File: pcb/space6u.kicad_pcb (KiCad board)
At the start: 2 copper layers, 116.7 x 45.2 mm, 7 parts, among them U1 Seeeduino Xiao rp2040

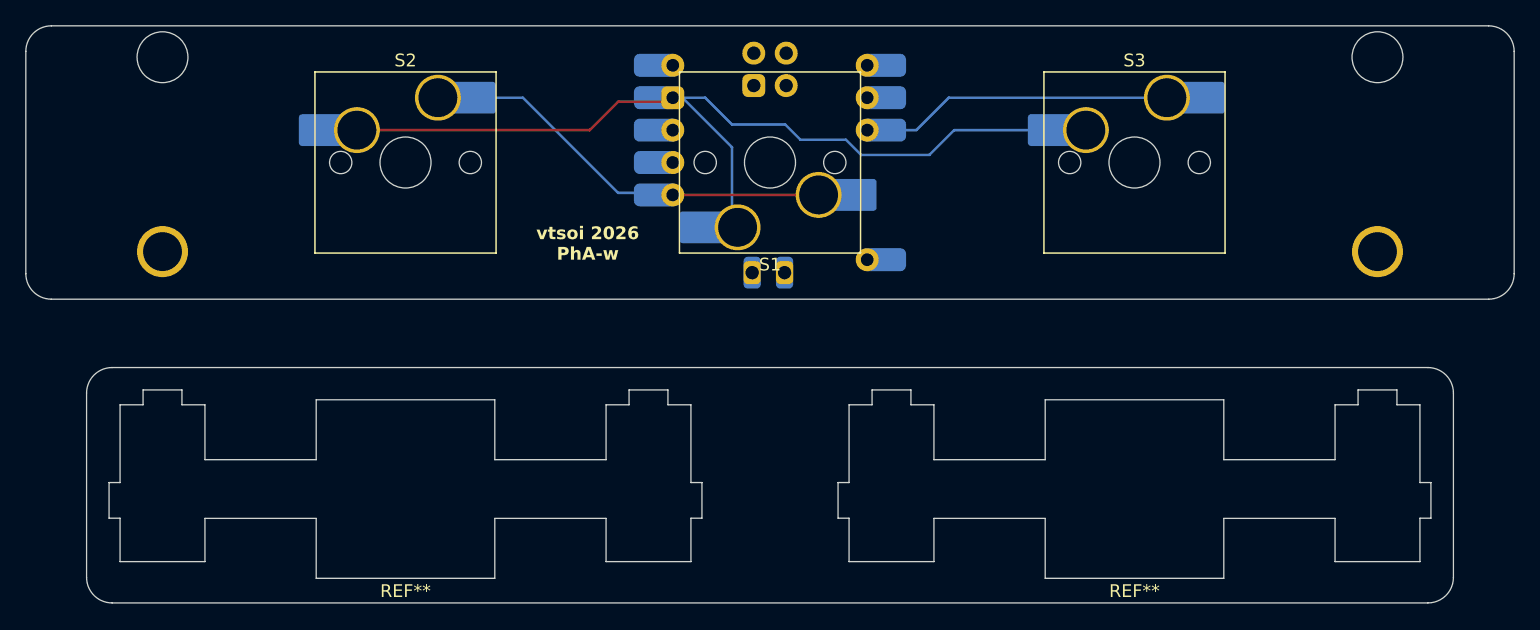
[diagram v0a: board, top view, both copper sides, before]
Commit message: plate and case files
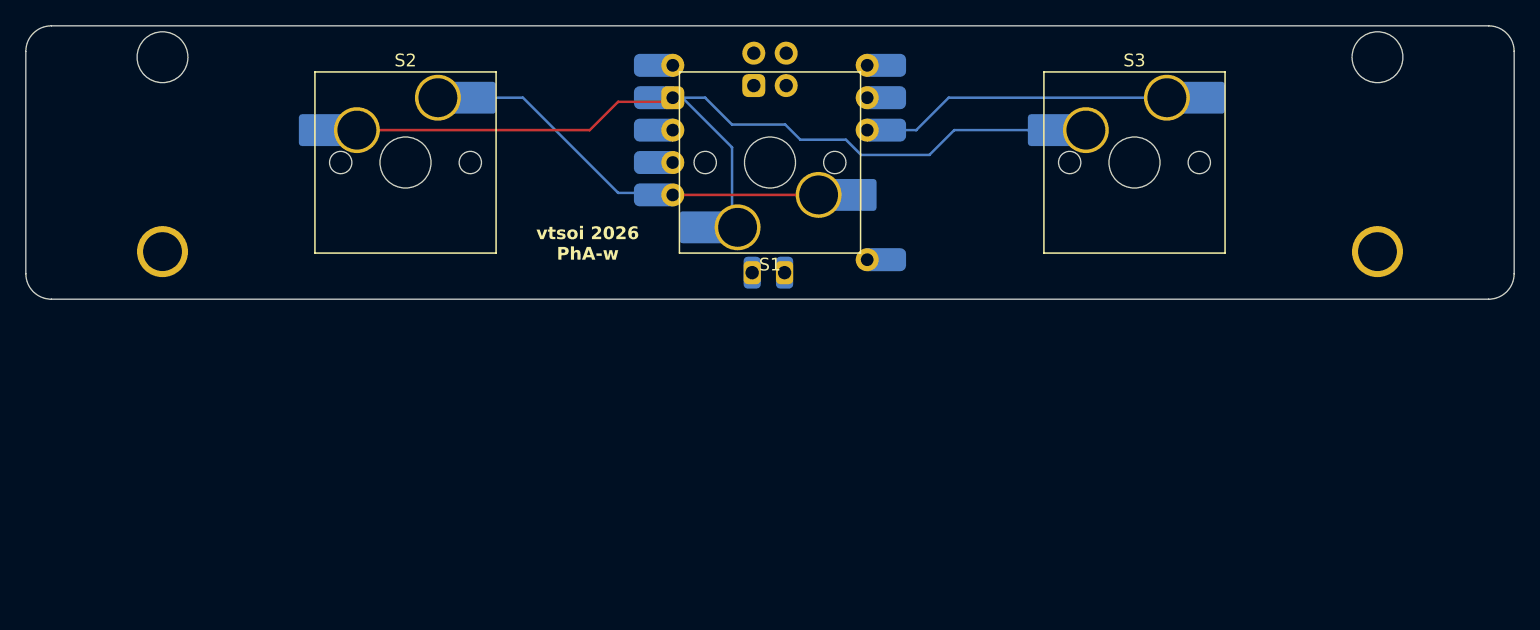
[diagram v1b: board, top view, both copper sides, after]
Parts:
- removed the REF** at (109.5, 88.7)
- removed the REF** at (166.7, 88.7)
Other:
- board size 116.7 x 45.2 mm -> 116.7 x 21.4 mm
